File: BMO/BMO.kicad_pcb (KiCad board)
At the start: 4 copper layers, 82 x 89.5 mm, 129 parts, among them J1 EXT, J10 USB_C_Receptacle_USB2.0_16P, J11 BAT, J12 Conn_01x06, J13 SERVO, J14 Conn_01x06, J2 Conn_ST_STDC14, J3 TOF1_VL53L0X, J4 TOF2_VL53L0X, J5 COULEUR_I2C, J6 NEOPIXEL, J7 LIDAR_X2, J8 OLED_I2C, J9 Conn_01x06, Q1 MMDT2907A-7-F, Q2 DMP1045U-7, Q3 DMN313DLT-7, SW1 USER, SW2 SW_Push, SW3 nQON, U1 STM32G474RBTx, U2 MPU-6050, U3 SN74AHCT1G125DBVR, U4 USBLC6-2SC6, U5 AP2112K-3.3, U6 BQ27220YZFR, U7 BQ25896RTW, U8 DRV8833PWPR, Y1 16MHz

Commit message: Mise à jour des fichiers PCB
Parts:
- added C45: 100n, Capacitor_SMD:C_0402_1005Metric, F.Cu at (154.8, 71.8)
- added TP10: TestPoint, TestPoint:TestPoint_Pad_D1.5mm, F.Cu at (137.5, 82.5)
- added TP11: TestPoint, TestPoint:TestPoint_Pad_D1.5mm, F.Cu at (156.6, 138.2)
- moved R30 15.1 mm to (137.0, 95.0)
- moved D5 15.0 mm to (140.0, 95.0)
- moved C18 15.0 mm to (173.1, 73.4), turned to 180 degrees
- moved U3 13.8 mm to (173.0, 76.0)
- moved R4 7.09 mm to (167.3, 68.5), turned to 0 degrees
- moved J2 5.87 mm to (171.0, 84.0), turned to 180 degrees
- moved TP8 5.41 mm to (146.0, 126.0)
- moved TP9 4.91 mm to (143.0, 116.0)
- moved R27 3.96 mm to (126.0, 138.0), turned to 90 degrees
- moved R29 3.83 mm to (122.0, 138.0), turned to 90 degrees
- moved C30 3.46 mm to (133.7, 112.2), turned to 0 degrees
- moved JP3 3.45 mm to (139.0, 103.2)
- moved TP1 3.32 mm to (125.0, 126.0)
- moved R6 3.30 mm to (118.0, 77.0)
- moved TP3 3.26 mm to (120.0, 131.0)
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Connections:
- J1 pad 8: /STM32G474RBT3/EXT_PC0 -> /STM32G474RBT3/BUZZER_TIM17_CH1
- U1 pad 58: /Motors/~{FAULT} -> /STM32G474RBT3/BUZZER_TIM17_CH1
- U1 pad 8: /STM32G474RBT3/EXT_PC0 -> /Motors/~{FAULT}
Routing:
- net Net-(J11-Pin_1): track 17.0 -> 0.00 mm
- net +3.3V: track 15.0 -> 0.00 mm
- net +5V: track 14.1 -> 0.00 mm
- net /Power/BAT: track 10.2 -> 0.00 mm
- net GND: track 4.23 -> 0.00 mm

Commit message: feat(pcb): update placement, fallback I2C, and route MCU, sensors, and external pins
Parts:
- moved TP10 4.34 mm to (135.0, 79.0)
- moved TP5 4.00 mm to (153.0, 126.0)
- moved C23 1.79 mm to (120.0, 111.0)
- moved R16 1.74 mm to (145.0, 135.0), turned to 180 degrees
- moved C37 1.64 mm to (139.0, 121.0)
- moved C36 1.64 mm to (139.0, 119.0)
- moved R15 1.54 mm to (123.0, 111.0)
- moved R2 1.48 mm to (160.0, 125.0)
- moved C5 1.43 mm to (154.0, 88.0)
- moved R23 1.35 mm to (140.0, 130.0)
- moved R25 1.28 mm to (133.0, 132.0)
- moved C39 1.12 mm to (152.0, 103.0)
- moved R10 1.00 mm to (160.0, 129.0)
- moved C11 1.00 mm to (138.0, 78.0)
- moved C12 1.00 mm to (138.0, 80.0)
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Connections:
- J1 pad 3: /STM32G474RBT3/EXT_PC7 -> /STM32G474RBT3/I2C3_SDA_ToF_TCS_MPU
- J1 pad 4: /STM32G474RBT3/EXT_PB12 -> /STM32G474RBT3/I2C3_SCL_ToF_TCS_MPU
- J1 pad 5: /STM32G474RBT3/EXT_PB13 -> /STM32G474RBT3/EXT_PB15
- J1 pad 6: /STM32G474RBT3/EXT_PB15 -> /STM32G474RBT3/EXT_PB13
- J1 pad 7: /STM32G474RBT3/EXT_PB11 -> /STM32G474RBT3/EXT_PB12
- J1 pad 8: /STM32G474RBT3/BUZZER_TIM17_CH1 -> /STM32G474RBT3/EXT_PB11
- J1 pad 9: /STM32G474RBT3/EXT_PC1 -> /STM32G474RBT3/BUZZER_TIM17_CH1
- U1 pad 39: /STM32G474RBT3/EXT_PC7 -> unconnected-(U1-PC7-Pad39)
- U1 pad 9: /STM32G474RBT3/EXT_PC1 -> unconnected-(U1-PC1-Pad9)
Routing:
- net /STM32G474RBT3/SWO: track 0.00 -> 16.7 mm
- net /STM32G474RBT3/SWDIO: track 0.00 -> 15.4 mm
- net /STM32G474RBT3/SWCLK: track 0.00 -> 15.0 mm
- net +5V: track 0.00 -> 7.92 mm
- net +3.3V: track 0.00 -> 2.31 mm
- net Net-(D3-K): track 0.00 -> 2.11 mm

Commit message: updated the shematic and routed the pcb
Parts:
- moved R8 4.00 mm to (140.0, 64.0)
- moved C1 3.52 mm to (154.0, 64.5)
- moved R7 3.00 mm to (145.0, 64.0)
- moved C21 2.78 mm to (149.2, 64.0)
- moved C7 1.79 mm to (143.5, 83.0), turned to 0 degrees
- moved C38 1.41 mm to (147.0, 103.0)
- moved L1 1.41 mm to (139.0, 84.0)
- moved C10 1.12 mm to (150.0, 70.0), turned to 90 degrees
- moved C6 1.12 mm to (145.0, 71.0), turned to -90 degrees
- moved C2 1.00 mm to (148.0, 67.0)
- moved C45 1.00 mm to (156.0, 71.0)
- moved TP10 1.00 mm to (134.0, 79.0)
- moved U4 1.00 mm to (150.0, 133.0)
- moved Y1 1.00 mm to (151.0, 67.0)
- moved C3 0.32 mm to (142.2, 79.8), turned to 0 degrees
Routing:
- net /STM32G474RBT3/I2C3_SCL_ToF_TCS_MPU: track 0.00 -> 112.0 mm, vias 0 -> 5
- net /Motors/SERVO_PINCE_TIM8_CH1: track 0.00 -> 64.2 mm, vias 0 -> 2
- net /STM32G474RBT3/I2C3_SDA_ToF_TCS_MPU: track 0.00 -> 60.1 mm
- net BOUT2: track 0.00 -> 56.9 mm, vias 0 -> 2
- net /Motors/ENC_L_A_TIM2_CH1: track 0.00 -> 55.1 mm, vias 0 -> 4
- net /STM32G474RBT3/BLE_En: track 0.00 -> 54.5 mm
- net /STM32G474RBT3/LIDAR_M_CTR_TIM16_CH1: track 0.00 -> 53.7 mm, vias 0 -> 2
- net /STM32G474RBT3/LIDARX2__USART1_RX: track 0.00 -> 51.8 mm, vias 0 -> 2
- net AOUT1: track 0.00 -> 51.8 mm, vias 0 -> 6
- net /STM32G474RBT3/I2C2_SDA_OLED: track 0.00 -> 50.5 mm, vias 0 -> 2
- net /STM32G474RBT3/BLE_USART3_RX: track 0.00 -> 49.9 mm
- net /Motors/ENC_L_B_TIM2_CH2: track 0.00 -> 48.5 mm, vias 0 -> 4
- net /STM32G474RBT3/BLE_USART3_TX: track 0.00 -> 47.5 mm
- net /STM32G474RBT3/I2C2_SCL_OLED: track 0.00 -> 45.1 mm, vias 0 -> 2
- net AOUT2: track 0.00 -> 44.3 mm, vias 0 -> 4
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- added copper zone on In1.Cu, net +3.3V
- added copper zone on B.Cu, net GND
- added copper zone on F.Cu, net GND
- added copper zone on In1.Cu, net GND

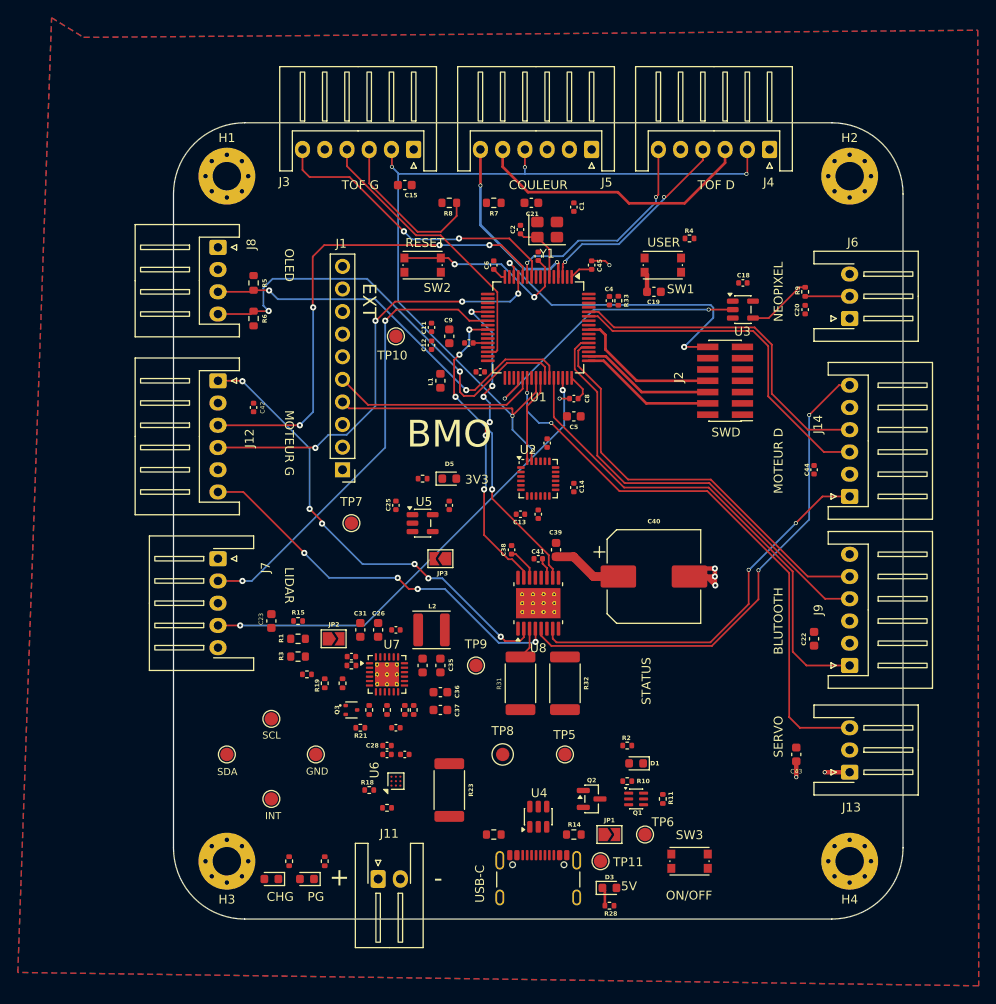
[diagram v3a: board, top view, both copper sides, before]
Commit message: feat(pcb): complete initial routing (v1) pending verification
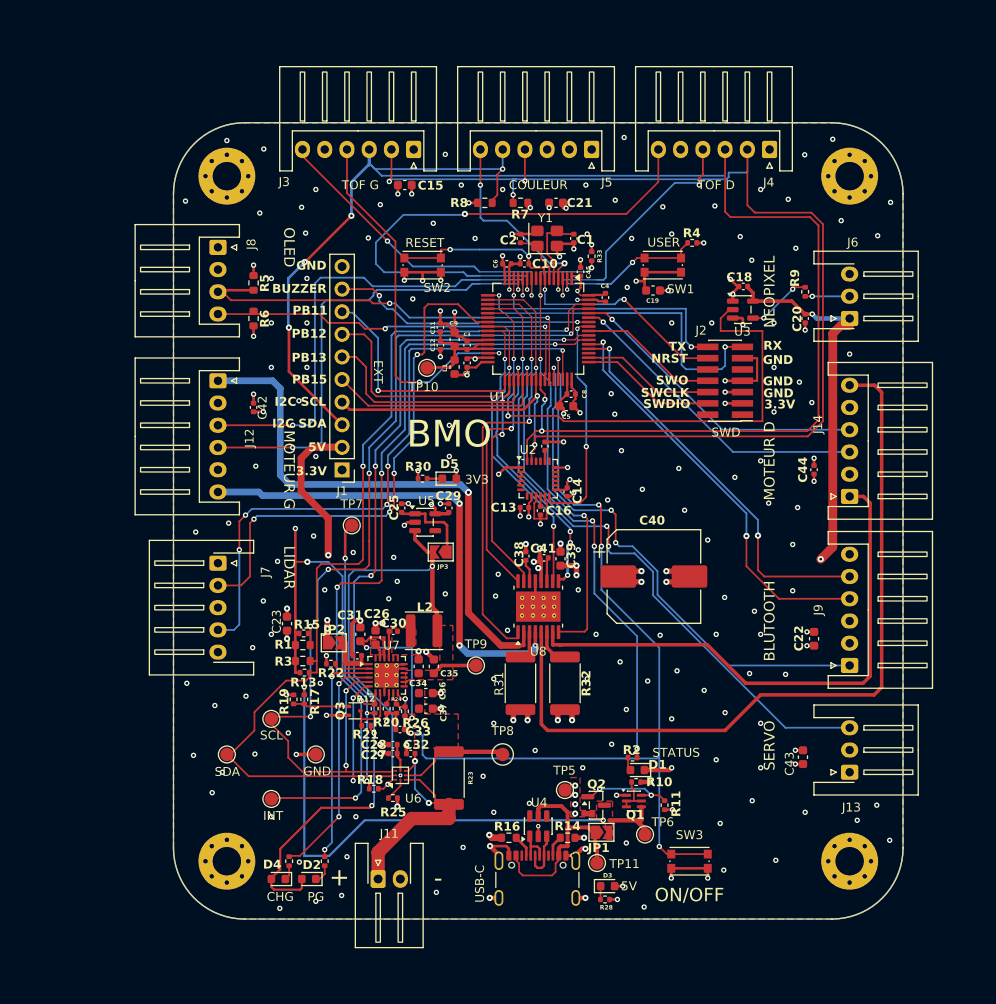
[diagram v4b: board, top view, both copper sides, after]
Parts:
- moved R33 5.83 mm to (156.0, 70.0)
- moved TP10 4.99 mm to (137.5, 82.5)
- moved R17 4.67 mm to (123.7, 119.8)
- moved R8 4.00 mm to (144.0, 64.0)
- moved TP5 4.00 mm to (153.0, 130.0)
- moved R19 3.94 mm to (122.5, 119.8)
- moved C1 3.52 mm to (154.0, 68.0)
- moved R7 3.00 mm to (148.0, 64.0)
- moved C21 2.78 mm to (152.0, 64.0)
- moved R22 2.31 mm to (126.7, 115.8)
- moved L1 2.23 mm to (140.6, 82.5)
- moved C23 1.79 mm to (121.8, 111.3)
- moved C7 1.79 mm to (142.0, 82.0), turned to -90 degrees
- moved C10 1.77 mm to (148.4, 70.8), turned to 180 degrees
- moved C38 1.75 mm to (148.6, 103.7)
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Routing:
- net /STM32G474RBT3/I2C3_SDA_ToF_TCS_MPU: track 60.1 -> 184.2 mm, vias 0 -> 6
- net /STM32G474RBT3/I2C1_SDA_Jauge: track 0.00 -> 115.7 mm, vias 0 -> 4
- net GND: track 19.2 -> 133.9 mm, vias 7 -> 196
- net /STM32G474RBT3/I2C1_SCL_Jauge: track 0.00 -> 108.2 mm, vias 0 -> 7
- net /Power/PWR_Bouton: track 0.00 -> 105.7 mm, vias 0 -> 6
- net +3.3V: track 9.57 -> 104.1 mm, vias 0 -> 31
- net /Power/CHARGER_INT: track 0.00 -> 89.8 mm, vias 0 -> 5
- net /Power/FG_GPOUT: track 0.00 -> 77.5 mm, vias 0 -> 4
- net SYS: track 0.00 -> 77.2 mm, vias 0 -> 3
- net +5V: track 7.92 -> 74.8 mm, vias 0 -> 37
- net VBUS: track 0.00 -> 62.3 mm, vias 0 -> 2
- net /STM32G474RBT3/LED_STATUS: track 0.00 -> 61.1 mm, vias 0 -> 4
- net /Motors/~{FAULT}: track 0.00 -> 54.5 mm, vias 0 -> 4
- net /Motors/~{SLEEP}: track 0.00 -> 50.5 mm, vias 0 -> 2
- net /STM32G474RBT3/I2C3_SCL_ToF_TCS_MPU: track 112.0 -> 154.9 mm
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- added copper zone on In2.Cu, net +3.3V
- added copper zone on F.Cu, net +5V
- added copper zone on In2.Cu, net +5V
- added copper zone on F.Cu, net /Power/BAT
- added copper zone on F.Cu, net Net-(C30-Pad2)
- added copper zone on F.Cu, net Net-(U7-PMID)
- added copper zone on F.Cu, net SYS
- added copper zone on F.Cu, net VBUS
- removed copper zone on In1.Cu, net +3.3V
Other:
- board text added: "3.3V"
- board text added: "BUZZER"
- board text added: "C10"
- board text added: "C16"
- board text added: "C27"
- board text added: "C29"
- board text added: "C3"
- board text added: "C30"
- board text added: "C32"
- board text added: "C33"
- board text added: "C34"
- board text added: "C7"
- board text added: "D2"
- board text added: "D4"
- board text added: "ENSEA 3A ESE v1.0 2627"
- board text added: "I2C SCL"
- board text added: "I2C SDA"
- board text added: "NRST"
- board text added: "PB11"
- board text added: "PB12"
- board text added: "PB13"
- board text added: "PB15"
- board text added: "R12"
- board text added: "R13"
- board text added: "R16"
- board text added: "R17"
- board text added: "R20"
- board text added: "R22"
- board text added: "R24"
- board text added: "R25"
- board text added: "R26"
- board text added: "R30"
- board text added: "RX"
- board text added: "SWCLK"
- board text added: "SWDIO"
- board text added: "SWO"
- board text added: "TX"
- board text added: "Yassin GARAFI Achraf AHAL Najd BEN SAAD"
- board text removed: "AVANT"
- board text removed: "ENSEA 3A ESE - v1.0 - 2026"
- board text removed: "N. BEN SAAD - A. AHAL - Y. GARAFI"

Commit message: refactor(pcb): optimize trace routing and clearances
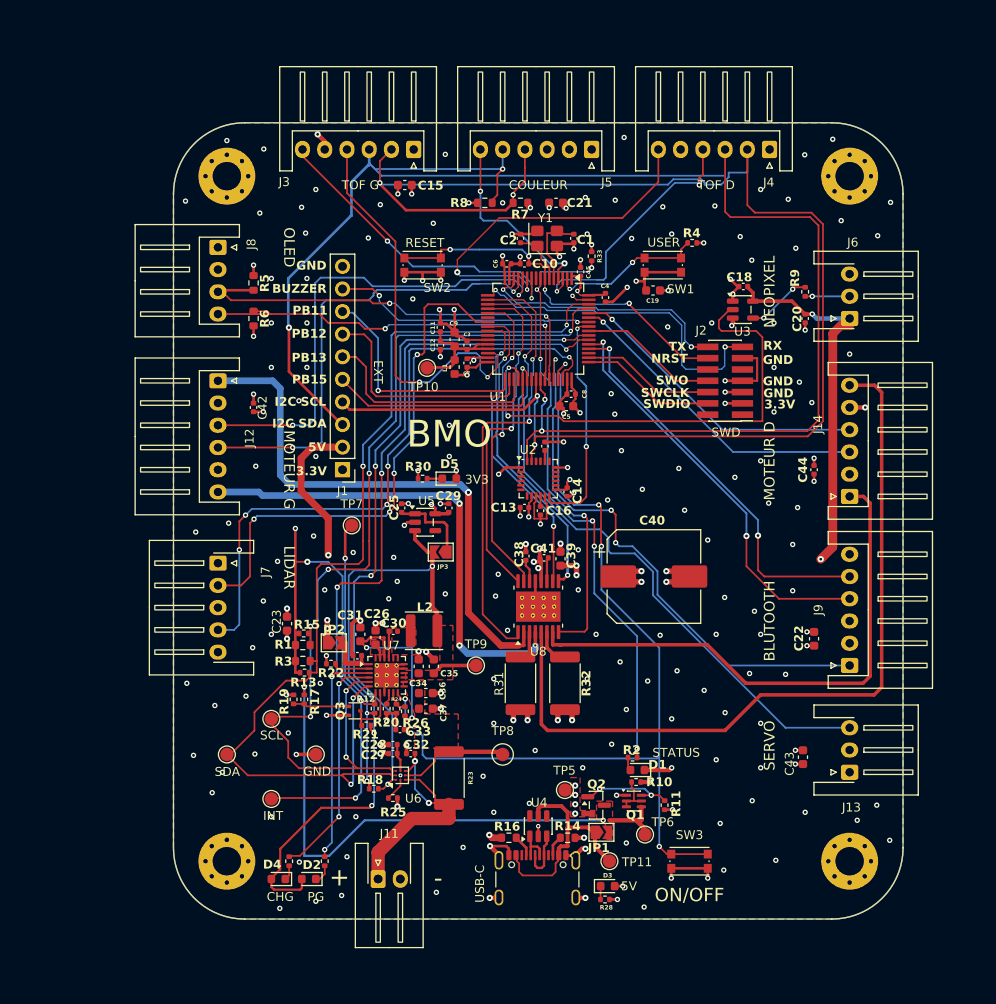
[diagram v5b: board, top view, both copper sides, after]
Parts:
- moved TP11 1.41 mm to (158.0, 138.0)
- moved J1 0.05 mm to (128.0, 94.0)
- moved J10 0.05 mm to (149.9, 141.0)
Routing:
- net /STM32G474RBT3/I2C3_SCL_ToF_TCS_MPU: track 154.9 -> 174.6 mm, vias 5 -> 4
- net /STM32G474RBT3/XSHUT_TOF2: track 60.4 -> 41.0 mm
- net GND: track 133.9 -> 140.2 mm
- net /STM32G474RBT3/TOF1_INT: track 40.9 -> 45.1 mm
- net /STM32G474RBT3/I2C2_SDA_OLED: track 42.6 -> 44.9 mm
- net /STM32G474RBT3/COLOR_INT: track 22.9 -> 20.7 mm, vias 3 -> 2
- net /STM32G474RBT3/BLE_En: track 59.7 -> 61.7 mm
- net /STM32G474RBT3/I2C1_SDA_Jauge: track 115.7 -> 117.1 mm
- net /STM32G474RBT3/I2C3_SDA_ToF_TCS_MPU: track 184.2 -> 182.9 mm, vias 6 -> 4
- net /STM32G474RBT3/LIDAR_M_CTR_TIM16_CH1: track 69.6 -> 70.7 mm
- net /STM32G474RBT3/VCP_RX: track 37.0 -> 36.1 mm
- net /STM32G474RBT3/NEOPIXEL: track 53.2 -> 54.0 mm
- net /Motors/SERVO_PINCE_TIM8_CH1: track 65.1 -> 64.4 mm, vias 3 -> 1
- net /STM32G474RBT3/USER_Bouton: track 17.3 -> 16.7 mm
- net /Motors/MOT_R_IN1_TIM3_CH3: track 34.8 -> 34.5 mm, vias 4 -> 2
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
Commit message: refactor(pcb): optimize clearances
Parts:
- moved L2 1.18 mm to (137.6, 111.0)
- moved C26 0.90 mm to (132.0, 112.0)
- moved R28 0.86 mm to (158.0, 143.0)
- moved C31 0.50 mm to (130.0, 112.0)
- moved R25 0.35 mm to (134.0, 131.0), turned to 180 degrees
- moved D3 0.28 mm to (158.0, 141.0)
- moved C35 0.26 mm to (138.0, 116.1)
- moved C34 0.16 mm to (136.4, 116.1)
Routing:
- net +3.3V: track 104.1 -> 93.0 mm, vias 30 -> 25
- net Net-(JP1-A): track 25.3 -> 18.3 mm, vias 0 -> 6
- net /Power/REGN: track 19.8 -> 16.3 mm, vias 2 -> 3
- net /STM32G474RBT3/VCP_RX: track 36.1 -> 33.4 mm
- net +5V: track 74.8 -> 72.6 mm, vias 37 -> 30
- net /STM32G474RBT3/NEOPIXEL: track 54.0 -> 55.5 mm
- net /Power/BAT: track 9.33 -> 10.8 mm
- net /STM32G474RBT3/I2C1_SCL_Jauge: track 108.2 -> 109.6 mm
- net Net-(U7-PMID): track 1.54 -> 2.82 mm
- net /Power/CHARGER_INT: track 90.3 -> 91.5 mm
- net /STM32G474RBT3/VCP_TX: track 27.6 -> 26.4 mm
- net /STM32G474RBT3/I2C1_SDA_Jauge: track 117.1 -> 118.0 mm
- net Net-(D3-K): track 1.50 -> 2.40 mm
- net SYS: track 77.2 -> 76.4 mm
- net /Power/STAT: track 26.1 -> 26.8 mm
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- added copper zone on In2.Cu, net Net-(JP1-A)
